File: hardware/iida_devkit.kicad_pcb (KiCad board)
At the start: 6 copper layers, 0 parts

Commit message: HW: Start laying out power section
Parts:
- added AE601: Antenna_Shield, iida-devkit:800MHz_PCB_ANT, F.Cu at (-138.3, 30.4)
- added C201: 1 µF, perfect_footprints:C_0201_0603Metric, F.Cu at (76.7, 38.3)
- added C202: 10 µF, Capacitor_SMD:C_0603_1608Metric, F.Cu at (-3.89, 23.7)
- added C203: 10 µF, Capacitor_SMD:C_0603_1608Metric, F.Cu at (2.71, 23.7)
- added C204: 4.7 µF, perfect_footprints:C_0402_1005Metric, F.Cu at (64.3, 75.9)
- added C205: 4.7 µF, perfect_footprints:C_0402_1005Metric, F.Cu at (66.9, 75.9)
- added C206: 100 µF, Capacitor_SMD:CP_Elec_6.3x3, F.Cu at (63.3, 30.8)
- added C207: 4.7 µF, perfect_footprints:C_0402_1005Metric, F.Cu at (70.4, 40.3)
- added C208: 1 µF, perfect_footprints:C_0201_0603Metric, F.Cu at (64.3, 79.5)
- added C209: 10 µF, Capacitor_SMD:C_0603_1608Metric, F.Cu at (67.8, 79.7)
- added C210: 10 µF, Capacitor_SMD:C_0603_1608Metric, F.Cu at (69.4, 79.7)
- added C211: 4.7 µF, perfect_footprints:C_0402_1005Metric, F.Cu at (69.6, 44.0)
- added C212: 1 µF, perfect_footprints:C_0201_0603Metric, F.Cu at (76.5, 81.6)
- added C213: 1 µF, perfect_footprints:C_0201_0603Metric, F.Cu at (66.4, 38.4)
- added C214: 22 µF, Capacitor_SMD:C_0603_1608Metric, F.Cu at (78.7, 79.8)
- added C215: 22 µF, Capacitor_SMD:C_0603_1608Metric, F.Cu at (80.3, 79.8)
- added C216: 22 µF, Capacitor_SMD:C_0603_1608Metric, F.Cu at (81.9, 79.8)
- added C301: 1 µF, perfect_footprints:C_0201_0603Metric, F.Cu at (-94.4, 96.2)
- added C302: 1 µF, perfect_footprints:C_0201_0603Metric, F.Cu at (-94.4, 97.8)
- added C303: 22 µF, Capacitor_SMD:C_0603_1608Metric, F.Cu at (-112.1, 103.3)
- added C304: 1 µF, perfect_footprints:C_0201_0603Metric, F.Cu at (-94.4, 99.4)
- added C305: 1 µF, perfect_footprints:C_0201_0603Metric, F.Cu at (-94.4, 101.0)
- added C306: 1 µF, perfect_footprints:C_0201_0603Metric, F.Cu at (-94.4, 102.7)
- added C307: 1 µF, perfect_footprints:C_0201_0603Metric, F.Cu at (-94.4, 104.3)
- added C308: 8 pF, perfect_footprints:C_0201_0603Metric, F.Cu at (-94.4, 105.9)
- added C309: 8 pF, perfect_footprints:C_0201_0603Metric, F.Cu at (-92.3, 96.2)
- added C310: 0.1 µF, perfect_footprints:C_0201_0603Metric, F.Cu at (-92.3, 97.8)
- added C311: 1 µF, perfect_footprints:C_0201_0603Metric, F.Cu at (-92.3, 99.4)
- added C312: 22 µF, Capacitor_SMD:C_0603_1608Metric, F.Cu at (-112.1, 105.8)
- added C313: 8 pF, perfect_footprints:C_0201_0603Metric, F.Cu at (-92.3, 101.0)
- added C314: 8 pF, perfect_footprints:C_0201_0603Metric, F.Cu at (-92.3, 102.7)
- added C315: 1 µF, perfect_footprints:C_0201_0603Metric, F.Cu at (-92.3, 104.3)
- added C401: 1 µF, perfect_footprints:C_0201_0603Metric, F.Cu at (-77.9, 89.0)
- added C402: 1 µF, perfect_footprints:C_0201_0603Metric, F.Cu at (-77.9, 90.7)
- added C403: 1 µF, perfect_footprints:C_0201_0603Metric, F.Cu at (-77.9, 92.3)
- added C404: 1 µF, perfect_footprints:C_0201_0603Metric, F.Cu at (-77.9, 93.9)
- added C405: 1 µF, perfect_footprints:C_0201_0603Metric, F.Cu at (-77.9, 95.5)
- added C501: 100 µF, Capacitor_SMD:CP_Elec_6.3x3, F.Cu at (-109.0, 68.4)
- added C502: 1 µF, perfect_footprints:C_0201_0603Metric, F.Cu at (-97.9, 64.1)
- added C503: 22 µF, Capacitor_SMD:C_0603_1608Metric, F.Cu at (-112.2, 73.7)
- added C504: 1 µF, perfect_footprints:C_0201_0603Metric, F.Cu at (-97.9, 65.7)
- added C505: 0.1 µF, perfect_footprints:C_0201_0603Metric, F.Cu at (-97.9, 67.3)
- added C506: 10000 pF, perfect_footprints:C_0201_0603Metric, F.Cu at (-97.9, 68.9)
- added C507: 1 µF, perfect_footprints:C_0201_0603Metric, F.Cu at (-97.9, 70.5)
- added C508: 100 pF, perfect_footprints:C_0201_0603Metric, F.Cu at (-97.9, 72.1)
- added C509: 10000 pF, perfect_footprints:C_0201_0603Metric, F.Cu at (-97.9, 73.7)
- added C510: 1 µF, perfect_footprints:C_0201_0603Metric, F.Cu at (-97.9, 75.3)
- added C511: 33 pF, perfect_footprints:C_0201_0603Metric, F.Cu at (-95.8, 64.1)
- added C512: 33 pF, perfect_footprints:C_0201_0603Metric, F.Cu at (-95.8, 65.7)
- added C513: 33 pF, perfect_footprints:C_0201_0603Metric, F.Cu at (-95.8, 67.3)
- added C601: 1.1 pF, perfect_footprints:C_0402_1005Metric, F.Cu at (-137.6, 32.9)
- added C602: 36 pF, perfect_footprints:C_0201_0603Metric, F.Cu at (-116.9, 32.7)
- added C603: 0.33 pF, perfect_footprints:C_0402_1005Metric, F.Cu at (-137.6, 34.9)
- added C604: 36 pF, perfect_footprints:C_0201_0603Metric, F.Cu at (-116.9, 34.3)
- added C605: 1.1 pF, perfect_footprints:C_0402_1005Metric, F.Cu at (-137.6, 36.8)
- added D201: SMAJ5.0A, Diode_SMD:D_SMA, F.Cu at (86.8, 30.8)
- added D202: SMAJ5.0A, Diode_SMD:D_SMA, F.Cu at (86.8, 43.0)
- added D203: DT1240A-08LP3810, Package_DFN_QFN:Diodes_UDFN3810-9_TYPE_B, F.Cu at (-7.19, 18.5)
- added D204: SMAJ5.0A, Diode_SMD:D_SMA, F.Cu at (0.31, 16.4)
- added D205: RED, LED_SMD:LED_0603_1608Metric, F.Cu at (71.3, 48.0)
- added D206: RED, LED_SMD:LED_0603_1608Metric, F.Cu at (-85.0, 141.7)
- added D207: RED, LED_SMD:LED_0603_1608Metric, F.Cu at (73.0, 48.0)
- added D208: RED, LED_SMD:LED_0603_1608Metric, F.Cu at (74.7, 48.0)
- added D401: RED, LED_SMD:LED_0603_1608Metric, F.Cu at (-66.4, 93.3)
- added D402: RED, LED_SMD:LED_0603_1608Metric, F.Cu at (-66.4, 95.9)
- added D403: RED, LED_SMD:LED_0603_1608Metric, F.Cu at (-66.4, 98.5)
- added D501: RED, LED_SMD:LED_0603_1608Metric, F.Cu at (-86.6, 70.5)
- added D502: RED, LED_SMD:LED_0603_1608Metric, F.Cu at (-86.6, 73.0)
- added D503: DT1240A-08LP3810, Package_DFN_QFN:Diodes_UDFN3810-9_TYPE_B, F.Cu at (-82.5, 66.1)
- added D601: DF2B5M4CT,L3F, Diode_SMD:D_SOD-882D, F.Cu at (-114.4, 33.0)
- added F201: 1.5 A, Fuse:Fuse_0805_2012Metric, F.Cu at (81.3, 42.2)
- added F202: 1.5 A, Fuse:Fuse_0805_2012Metric, F.Cu at (-0.63, 21.7)
- added FB501: BLM21BB201SH1D, Inductor_SMD:L_0805_2012Metric, F.Cu at (-101.5, 72.8)
- added FID101: Fiducial, Fiducial:Fiducial_1mm_Mask3mm, F.Cu at (-113.8, -81.4)
- added FID102: Fiducial, Fiducial:Fiducial_1mm_Mask3mm, F.Cu at (-113.8, -76.9)
- added FID103: Fiducial, Fiducial:Fiducial_1mm_Mask3mm, F.Cu at (-113.8, -72.3)
- added H101: MountingHole_Pad, MountingHole:MountingHole_5.3mm_M5_Pad_Via, F.Cu at (-122.2, -77.6)
- added H102: MountingHole_Pad, MountingHole:MountingHole_5.3mm_M5_Pad_Via, F.Cu at (-122.2, -65.5)
- added H103: MountingHole_Pad, MountingHole:MountingHole_5.3mm_M5_Pad_Via, F.Cu at (-122.2, -53.3)
- added H104: MountingHole_Pad, MountingHole:MountingHole_5.3mm_M5_Pad_Via, F.Cu at (-122.2, -41.2)
- added J201: B2B-XH-A, Connector_JST:JST_XH_B2B-XH-A_1x02_P2.50mm_Vertical, F.Cu at (84.8, 35.7)
- added J202: USB4105-GF-A, Connector_USB:USB_C_Receptacle_GCT_USB4105-xx-A_16P_TopMnt_Horizontal, F.Cu at (-7.99, 12.0)
- added J203: PRPC001DAAN-RC, Connector_PinHeader_2.54mm:PinHeader_1x02_P2.54mm_Vertical, F.Cu at (73.6, 27.3)
- added J204: PRPC001DAAN-RC, Connector_PinHeader_2.54mm:PinHeader_1x02_P2.54mm_Vertical, F.Cu at (3.68, 26.5)
- added J205: 61300111121, Connector_PinHeader_2.54mm:PinHeader_1x01_P2.54mm_Vertical, F.Cu at (73.9, 84.2)
- added J206: 61300111121, Connector_PinHeader_2.54mm:PinHeader_1x01_P2.54mm_Vertical, F.Cu at (-63.7, 145.9)
- added J207: 61300111121, Connector_PinHeader_2.54mm:PinHeader_1x01_P2.54mm_Vertical, F.Cu at (-63.7, 150.4)
- added J208: PRPC001DAAN-RC, Connector_PinHeader_2.54mm:PinHeader_1x02_P2.54mm_Vertical, F.Cu at (-87.6, 140.0)
- added J209: PRPC001DAAN-RC, Connector_PinHeader_2.54mm:PinHeader_1x02_P2.54mm_Vertical, F.Cu at (83.1, 75.9)
- added J301: TC2050, Connector:Tag-Connect_TC2050-IDC-NL_2x05_P1.27mm_Vertical_with_bottom_clip, F.Cu at (-113.1, 98.7)
- added J302: 61300611121, Connector_PinHeader_2.54mm:PinHeader_1x06_P2.54mm_Vertical, F.Cu at (-117.0, 80.4)
- added J303: 61300611121, Connector_PinHeader_2.54mm:PinHeader_1x06_P2.54mm_Vertical, F.Cu at (-112.4, 80.4)
- added J304: 61300611121, Connector_PinHeader_2.54mm:PinHeader_1x06_P2.54mm_Vertical, F.Cu at (-107.9, 80.4)
- added J305: 61300611121, Connector_PinHeader_2.54mm:PinHeader_1x06_P2.54mm_Vertical, F.Cu at (-103.3, 80.4)
- added J306: 61300611121, Connector_PinHeader_2.54mm:PinHeader_1x06_P2.54mm_Vertical, F.Cu at (-98.7, 80.4)
- added J501: SIM8066-6-1-14-01-A, GCT:SIM8066-6-1-14-01-A, F.Cu at (-106.6, 52.4)
- added J601: SMA 132134, Connector_Coaxial:SMA_Amphenol_132134-11_Vertical, F.Cu at (-122.6, 36.6)
- added JP301: SolderJumper_2_Open, Jumper:SolderJumper-2_P1.3mm_Open_TrianglePad1.0x1.5mm, F.Cu at (-104.6, 108.5)
- added L201: 1 µH, Inductor_SMD:L_Changjiang_FTC404020S, F.Cu at (73.9, 74.5)
- added L601: 36 nH, perfect_footprints:L_0402_1005Metric, F.Cu at (-137.6, 38.8)
- added L602: 1 nH, perfect_footprints:L_0402_1005Metric, F.Cu at (-134.7, 32.9)
- added L603: 110 nH, perfect_footprints:L_0402_1005Metric, F.Cu at (-134.7, 34.9)
- added L604: 1 nH, perfect_footprints:L_0402_1005Metric, F.Cu at (-134.7, 36.8)
- added L605: 36 nH, perfect_footprints:L_0402_1005Metric, F.Cu at (-134.7, 38.8)
- added Q201: IRLML6401, Package_TO_SOT_SMD:SOT-23-3, F.Cu at (79.1, 36.9)
- added Q202: DMN2005, Package_SON:Diodes_PowerDI3333-8, F.Cu at (74.5, 31.1)
- added Q203: DMN2005, Package_SON:Diodes_PowerDI3333-8, F.Cu at (70.2, 31.1)
- added Q301: BSS806NH, Package_TO_SOT_SMD:SOT-23-3, F.Cu at (-116.8, 108.8)
- added Q501: BSS806NH, Package_TO_SOT_SMD:SOT-23-3, F.Cu at (-116.8, 45.5)
- added Q502: IRLML6401, Package_TO_SOT_SMD:SOT-23-3, F.Cu at (-116.8, 49.9)
- added Q503: BSS806NH, Package_TO_SOT_SMD:SOT-23-3, F.Cu at (-116.8, 54.4)
- added Q504: BSS806NH, Package_TO_SOT_SMD:SOT-23-3, F.Cu at (-116.8, 58.8)
- added Q505: BSS806NH, Package_TO_SOT_SMD:SOT-23-3, F.Cu at (-116.8, 63.3)
- added Q506: BSS806NH, Package_TO_SOT_SMD:SOT-23-3, F.Cu at (-116.8, 67.7)
- added R101: 0 Ω, Resistor_SMD:R_1206_3216Metric, F.Cu at (-113.3, -68.4)
- added R201: 5.1 kΩ, perfect_footprints:R_0402_1005Metric, F.Cu at (-14.0, 15.8)
- added R202: 5.1 kΩ, perfect_footprints:R_0402_1005Metric, F.Cu at (-2.09, 15.8)
- added R203: 330 Ω, perfect_footprints:R_0201_0603Metric, F.Cu at (76.7, 37.6)
- added R204: 82 mΩ, Resistor_SMD:R_1206_3216Metric, F.Cu at (79.1, 31.5)
- added R205: 0 Ω, Resistor_SMD:R_0805_2012Metric, F.Cu at (-0.61, 23.7)
- added R206: 2.2 kΩ, perfect_footprints:R_0201_0603Metric, F.Cu at (75.6, 38.3)
- added R207: 180 kΩ, perfect_footprints:R_0201_0603Metric, F.Cu at (64.3, 80.2)
- added R208: 10 kΩ, perfect_footprints:R_0201_0603Metric, F.Cu at (73.8, 39.1)
- added R209: 2.2 kΩ, perfect_footprints:R_0201_0603Metric, F.Cu at (73.8, 40.5)
- added R210: 0 Ω, perfect_footprints:R_0201_0603Metric, F.Cu at (70.9, 80.7)
- added R211: 0 Ω, perfect_footprints:R_0201_0603Metric, F.Cu at (71.6, 80.7)
- added R212: 2.2 kΩ, perfect_footprints:R_0201_0603Metric, F.Cu at (71.8, 45.8)
- added R213: 2.2 kΩ, perfect_footprints:R_0201_0603Metric, F.Cu at (-85.0, 139.6)
- added R214: 2.2 kΩ, perfect_footprints:R_0201_0603Metric, F.Cu at (72.5, 45.8)
- added R215: 2.2 kΩ, perfect_footprints:R_0201_0603Metric, F.Cu at (73.8, 39.8)
- added R216: 1.02 MΩ, perfect_footprints:R_0201_0603Metric, F.Cu at (77.6, 79.6)
- added R217: 180 kΩ, perfect_footprints:R_0201_0603Metric, F.Cu at (76.9, 80.2)
- added R218: 22 Ω, perfect_footprints:R_0201_0603Metric, F.Cu at (64.0, 41.4)
- added R219: 0 Ω, Resistor_SMD:R_0805_2012Metric, F.Cu at (84.4, 78.7)
- added R301: 180 kΩ, perfect_footprints:R_0201_0603Metric, F.Cu at (-92.3, 105.9)
- added R302: 10 kΩ, perfect_footprints:R_0201_0603Metric, F.Cu at (-90.3, 96.2)
- added R303: 330 Ω, perfect_footprints:R_0201_0603Metric, F.Cu at (-90.3, 97.8)
- added R304: 330 Ω, perfect_footprints:R_0201_0603Metric, F.Cu at (-90.3, 99.4)
- added R305: 2.2 kΩ, perfect_footprints:R_0201_0603Metric, F.Cu at (-90.3, 101.0)
- added R306: 2.2 kΩ, perfect_footprints:R_0201_0603Metric, F.Cu at (-90.3, 102.7)
- added R307: 10 kΩ, perfect_footprints:R_0201_0603Metric, F.Cu at (-90.3, 104.3)
- added R308: 10 kΩ, perfect_footprints:R_0201_0603Metric, F.Cu at (-90.3, 105.9)
- added R309: 22 Ω, perfect_footprints:R_0201_0603Metric, F.Cu at (-88.2, 96.2)
- added R310: 22 Ω, perfect_footprints:R_0201_0603Metric, F.Cu at (-88.2, 97.8)
- added R311: 22 Ω, perfect_footprints:R_0201_0603Metric, F.Cu at (-88.2, 99.4)
- added R312: 22 Ω, perfect_footprints:R_0201_0603Metric, F.Cu at (-88.2, 101.0)
- added R313: 22 Ω, perfect_footprints:R_0201_0603Metric, F.Cu at (-88.2, 102.7)
- added R314: 22 Ω, perfect_footprints:R_0201_0603Metric, F.Cu at (-88.2, 104.3)
- added R315: 22 Ω, perfect_footprints:R_0201_0603Metric, F.Cu at (-88.2, 105.9)
- added R316: 22 Ω, perfect_footprints:R_0201_0603Metric, F.Cu at (-86.1, 96.2)
- added R317: 22 Ω, perfect_footprints:R_0201_0603Metric, F.Cu at (-86.1, 97.8)
- added R318: 0 Ω, Resistor_SMD:R_0805_2012Metric, F.Cu at (-111.9, 108.5)
- added R319: 22 Ω, perfect_footprints:R_0201_0603Metric, F.Cu at (-86.1, 99.4)
- added R320: 330 Ω, perfect_footprints:R_0201_0603Metric, F.Cu at (-86.1, 101.0)
- added R321: 10 kΩ, perfect_footprints:R_0201_0603Metric, F.Cu at (-86.1, 102.7)
- added R401: 180 kΩ, perfect_footprints:R_0201_0603Metric, F.Cu at (-77.9, 97.1)
- added R402: 22 Ω, perfect_footprints:R_0201_0603Metric, F.Cu at (-77.9, 98.7)
- added R403: 22 Ω, perfect_footprints:R_0201_0603Metric, F.Cu at (-75.8, 89.0)
- added R404: 22 Ω, perfect_footprints:R_0201_0603Metric, F.Cu at (-75.8, 90.7)
- added R405: 22 Ω, perfect_footprints:R_0201_0603Metric, F.Cu at (-75.8, 92.3)
- added R406: 22 Ω, perfect_footprints:R_0201_0603Metric, F.Cu at (-75.8, 93.9)
- added R407: 22 Ω, perfect_footprints:R_0201_0603Metric, F.Cu at (-75.8, 95.5)
- added R408: 22 Ω, perfect_footprints:R_0201_0603Metric, F.Cu at (-75.8, 97.1)
- added R409: 22 Ω, perfect_footprints:R_0201_0603Metric, F.Cu at (-75.8, 98.7)
- added R410: 2.2 kΩ, perfect_footprints:R_0201_0603Metric, F.Cu at (-73.8, 89.0)
- added R411: 2.2 kΩ, perfect_footprints:R_0201_0603Metric, F.Cu at (-73.8, 90.7)
- added R412: 2.2 kΩ, perfect_footprints:R_0201_0603Metric, F.Cu at (-73.8, 92.3)
- added R413: 180 kΩ, perfect_footprints:R_0201_0603Metric, F.Cu at (-73.8, 93.9)
- added R414: 180 kΩ, perfect_footprints:R_0201_0603Metric, F.Cu at (-73.8, 95.5)
- added R415: 22 Ω, perfect_footprints:R_0201_0603Metric, F.Cu at (-73.8, 97.1)
- added R416: 180 kΩ, perfect_footprints:R_0201_0603Metric, F.Cu at (-73.8, 98.7)
- added R501: 180 kΩ, perfect_footprints:R_0201_0603Metric, F.Cu at (-95.8, 68.9)
- added R502: 180 kΩ, perfect_footprints:R_0201_0603Metric, F.Cu at (-95.8, 70.5)
- added R503: 330 Ω, perfect_footprints:R_0201_0603Metric, F.Cu at (-95.8, 72.1)
- added R504: 0 Ω, Resistor_SMD:R_0805_2012Metric, F.Cu at (-86.4, 64.7)
- added R505: 0 Ω, Resistor_SMD:R_0805_2012Metric, F.Cu at (-86.4, 67.7)
- added R506: 180 kΩ, perfect_footprints:R_0201_0603Metric, F.Cu at (-95.8, 73.7)
- added R507: 330 Ω, perfect_footprints:R_0201_0603Metric, F.Cu at (-95.8, 75.3)
- added R508: 330 Ω, perfect_footprints:R_0201_0603Metric, F.Cu at (-93.8, 64.1)
- added R509: 22 Ω, perfect_footprints:R_0201_0603Metric, F.Cu at (-93.8, 65.7)
- added R510: 22 Ω, perfect_footprints:R_0201_0603Metric, F.Cu at (-93.8, 67.3)
- added R511: 22 Ω, perfect_footprints:R_0201_0603Metric, F.Cu at (-93.8, 68.9)
- added R512: 22 Ω, perfect_footprints:R_0201_0603Metric, F.Cu at (-93.8, 70.5)
- added R513: 180 kΩ, perfect_footprints:R_0201_0603Metric, F.Cu at (-93.8, 72.1)
- added R514: 330 Ω, perfect_footprints:R_0201_0603Metric, F.Cu at (-93.8, 73.7)
- added R515: 180 kΩ, perfect_footprints:R_0201_0603Metric, F.Cu at (-93.8, 75.3)
- added R516: 22 Ω, perfect_footprints:R_0201_0603Metric, F.Cu at (-91.7, 64.1)
- added R517: 22 Ω, perfect_footprints:R_0201_0603Metric, F.Cu at (-91.7, 65.7)
- added R518: 22 Ω, perfect_footprints:R_0201_0603Metric, F.Cu at (-91.7, 67.3)
- added R519: 180 kΩ, perfect_footprints:R_0201_0603Metric, F.Cu at (-91.7, 68.9)
- added R520: 330 Ω, perfect_footprints:R_0201_0603Metric, F.Cu at (-91.7, 70.5)
- added R521: 2.2 kΩ, perfect_footprints:R_0201_0603Metric, F.Cu at (-91.7, 72.1)
- added R522: 180 kΩ, perfect_footprints:R_0201_0603Metric, F.Cu at (-91.7, 73.7)
- added R523: 330 Ω, perfect_footprints:R_0201_0603Metric, F.Cu at (-91.7, 75.3)
- added R524: 2.2 kΩ, perfect_footprints:R_0201_0603Metric, F.Cu at (-89.6, 64.1)
- added R525: 180 kΩ, perfect_footprints:R_0201_0603Metric, F.Cu at (-89.6, 65.7)
- added R526: 180 kΩ, perfect_footprints:R_0201_0603Metric, F.Cu at (-89.6, 67.3)
- added R601: 0 Ω, perfect_footprints:R_0402_1005Metric, F.Cu at (-131.7, 32.9)
- added R602: 0 Ω, perfect_footprints:R_0402_1005Metric, F.Cu at (-131.7, 34.9)
- added R603: 0 Ω, perfect_footprints:R_0402_1005Metric, F.Cu at (-131.7, 36.8)
- added R604: 0 Ω, perfect_footprints:R_0402_1005Metric, F.Cu at (-131.7, 38.8)
- added R605: 0 Ω, perfect_footprints:R_0402_1005Metric, F.Cu at (-128.8, 32.9)
- added R606: 0 Ω, perfect_footprints:R_0402_1005Metric, F.Cu at (-128.8, 34.9)
- added R607: 0 Ω, perfect_footprints:R_0402_1005Metric, F.Cu at (-128.8, 36.8)
- added R608: 0 Ω, perfect_footprints:R_0402_1005Metric, F.Cu at (-128.8, 38.8)
- added SW301: PTS645S, Button_Switch_SMD:SW_SPST_PTS645Sx43SMTR92, F.Cu at (-90.8, 82.1)
- added SW302: PTS645S, Button_Switch_SMD:SW_SPST_PTS645Sx43SMTR92, F.Cu at (-90.8, 89.9)
- added TP201: TestPoint, TestPoint:TestPoint_Pad_D1.0mm, B.Cu at (76.0, 30.1)
- added TP202: TestPoint, TestPoint:TestPoint_Pad_D1.0mm, B.Cu at (69.4, 29.4)
- added TP203: TestPoint, TestPoint:TestPoint_Pad_D1.0mm, B.Cu at (80.3, 77.2)
- added TP204: TestPoint, TestPoint:TestPoint_Pad_D1.0mm, B.Cu at (-1.69, 26.5)
- added TP205: TestPoint, TestPoint:TestPoint_Pad_D1.0mm, B.Cu at (63.3, 36.6)
- added U201: BQ29728DSER, Package_SON:WSON-6_1.5x1.5mm_P0.5mm, F.Cu at (76.4, 39.9)
- added U202: LM66200DRLR, Package_TO_SOT_SMD:SOT-583-8, F.Cu at (65.6, 77.8)
- added U203: MCP73833T-FCI/MF, Package_DFN_QFN:DFN-10-1EP_3x3mm_P0.5mm_EP1.58x2.35mm, F.Cu at (71.9, 43.0)
- added U204: TPS63020DSJR, Texas Instruments:TPS6302xDSJ, F.Cu at (73.9, 79.4)
- added U205: MAX17048G+T10, Package_DFN_QFN:TDFN-8-1EP_2x2mm_P0.5mm_EP0.8x1.2mm, F.Cu at (65.9, 40.4)
- added U301: STM32L552CET6, Package_QFP:LQFP-48_7x7mm_P0.5mm, F.Cu at (-101.5, 100.4)
- added U401: TCA9554PW, Package_SO:TSSOP-16_4.4x5mm_P0.65mm, F.Cu at (-74.2, 84.9)
- added U402: AT25SF081B-MAHB-T, Package_DFN_QFN:DFN-8-1EP_2x3mm_P0.5mm_EP0.61x2.2mm, F.Cu at (-70.6, 94.3)
- added U403: MCP9808T-E/MC, Package_DFN_QFN:DFN-8-1EP_3x2mm_P0.5mm_EP1.75x1.45mm, F.Cu at (-69.9, 90.2)
- added U404: M24256E-B, Package_SO:SOIC-8_3.9x4.9mm_P1.27mm, F.Cu at (-65.6, 85.0)
- added U405: SHT40-AD1B-R2, Sensor_Humidity:Sensirion_DFN-4_1.5x1.5mm_P0.8mm_SHT4x_NoCentralPad, F.Cu at (-70.7, 98.1)
- added U501: TXS0108E, Package_DFN_QFN:DHVQFN-20-1EP_2.5x4.5mm_P0.5mm_EP1x3mm, F.Cu at (-101.4, 68.0)
- added U502: BG770AGLAA-N06-SGNSA, Quectel:Quectel_BG77, F.Cu at (-89.9, 53.3)
- added Y301: ECS-160-9-37-CKM-TR3, Crystal:Crystal_SMD_3225-4Pin_3.2x2.5mm, F.Cu at (-116.7, 104.3)
- added Y302: ABS05-32.768KHZ-9-T, Crystal:Crystal_SMD_MicroCrystal_CM9V-T1A-2Pin_1.6x1.0mm, F.Cu at (-100.6, 108.3)
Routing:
- net CHASSIS: track 0.00 -> 33.8 mm, vias 0 -> 1
- net /Power/V_BUS_IN: track 0.00 -> 26.7 mm, vias 0 -> 2
- net /Power/C_{OUT}: track 0.00 -> 23.9 mm, vias 0 -> 2
- net /Power/D_{OUT}: track 0.00 -> 18.2 mm, vias 0 -> 2
- net /Power/VINA: track 0.00 -> 12.2 mm
- net /Power/CC1: track 0.00 -> 8.13 mm
- net Net-(D208-K): track 0.00 -> 7.92 mm
- net /Power/V_BUS: track 0.00 -> 7.48 mm, vias 0 -> 1
- net GND: track 0.00 -> 7.32 mm, vias 0 -> 85
- net /Microcontroller/USB.D+: track 0.00 -> 7.26 mm
- net /Power/CC2: track 0.00 -> 7.21 mm
- net /Microcontroller/USB.D-: track 0.00 -> 6.27 mm
- net /Power/GND_BAT: track 0.00 -> 4.34 mm
- net /Power/THERM: track 0.00 -> 3.85 mm
- net /Microcontroller/I2C.SCL: track 0.00 -> 3.46 mm, vias 0 -> 1
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- added copper zone on F.Cu, net /Power/GND_BAT
- added copper zone on F.Cu, net /Power/V_BAT
- added copper zone on F.Cu, net /Power/V_BAT_IN
- added copper zone on F.Cu, net /Power/V_OUT
- added copper zone on F.Cu, net /Power/V_SYS
- added copper zone on B.Cu, net GND
- added copper zone on F.Cu, net GND
- added copper zone on In1.Cu, net GND
- added copper zone on In3.Cu, net GND
- added copper zone on In4.Cu, net GND
- added copper zone on F.Cu, net Net-(J203-Pin_1)
- added copper zone on F.Cu, net Net-(L201-Pad1)
- added copper zone on F.Cu, net Net-(L201-Pad2)
- added copper zone on F.Cu, net Net-(Q201-D)
- added copper zone on F.Cu, net Net-(Q202-D)
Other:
- board text added: "+5V"
- board text added: "BAT+"
- board text added: "BAT-"
- board text added: "GND"

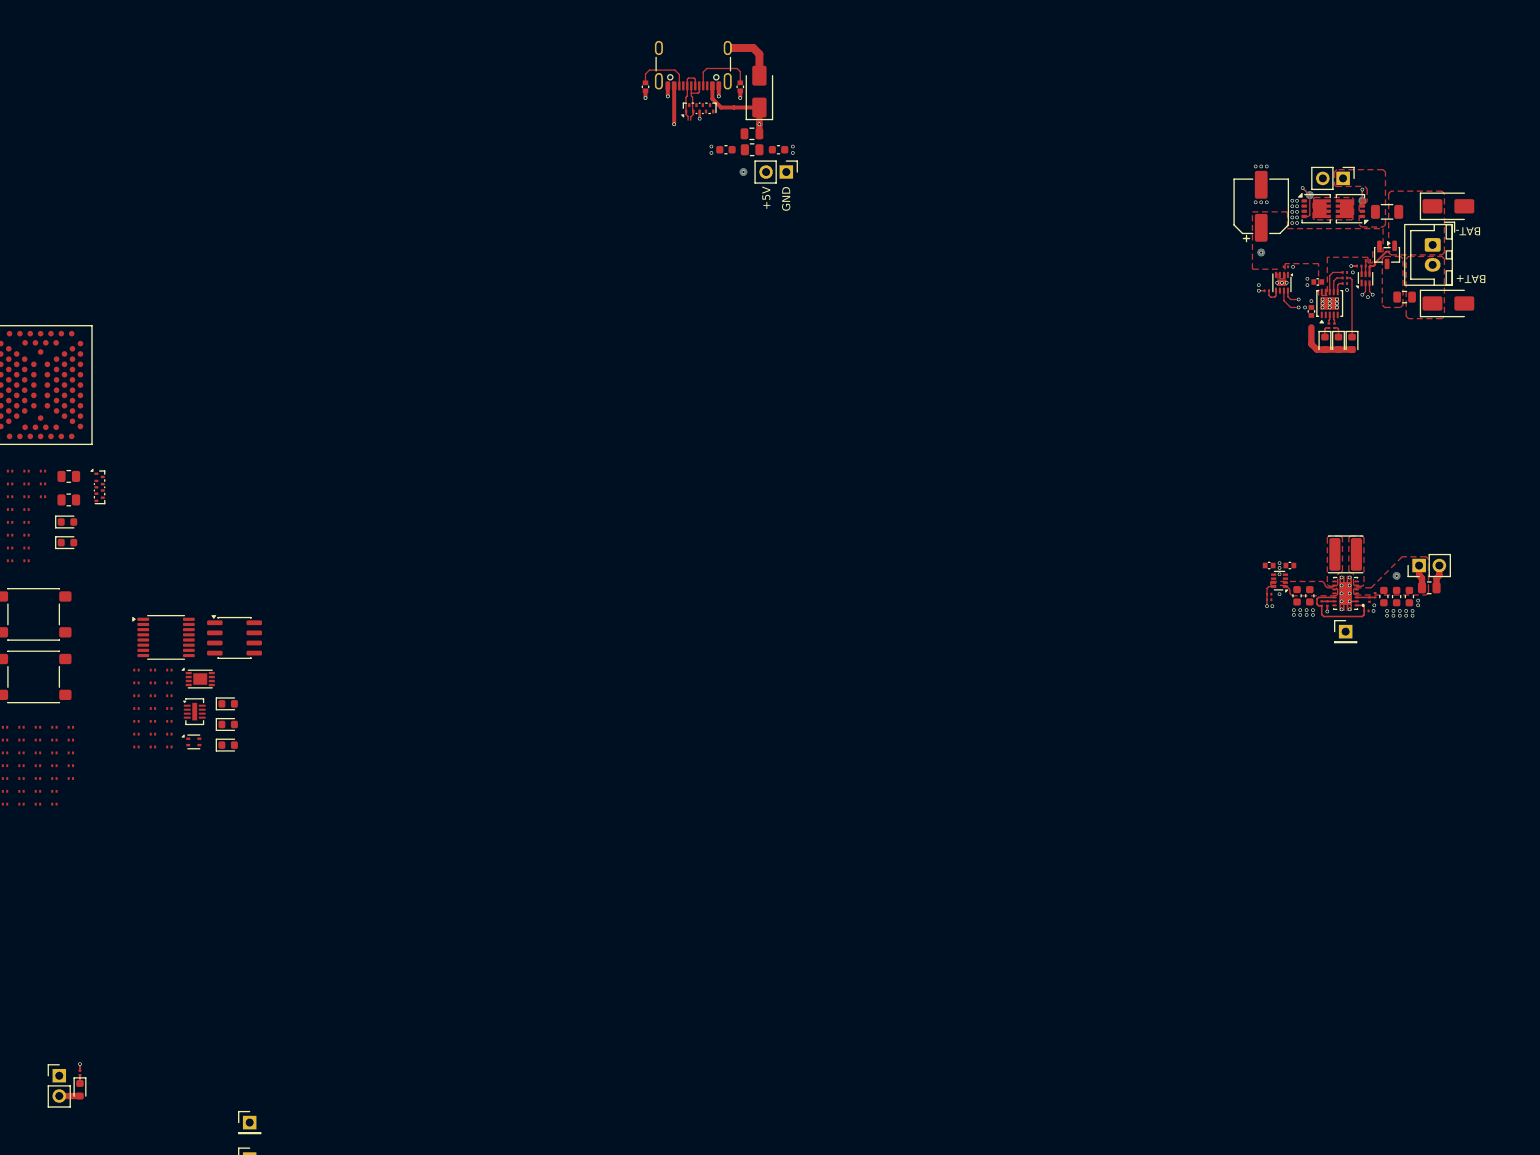
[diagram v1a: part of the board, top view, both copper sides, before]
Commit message: HW: Finish power layout
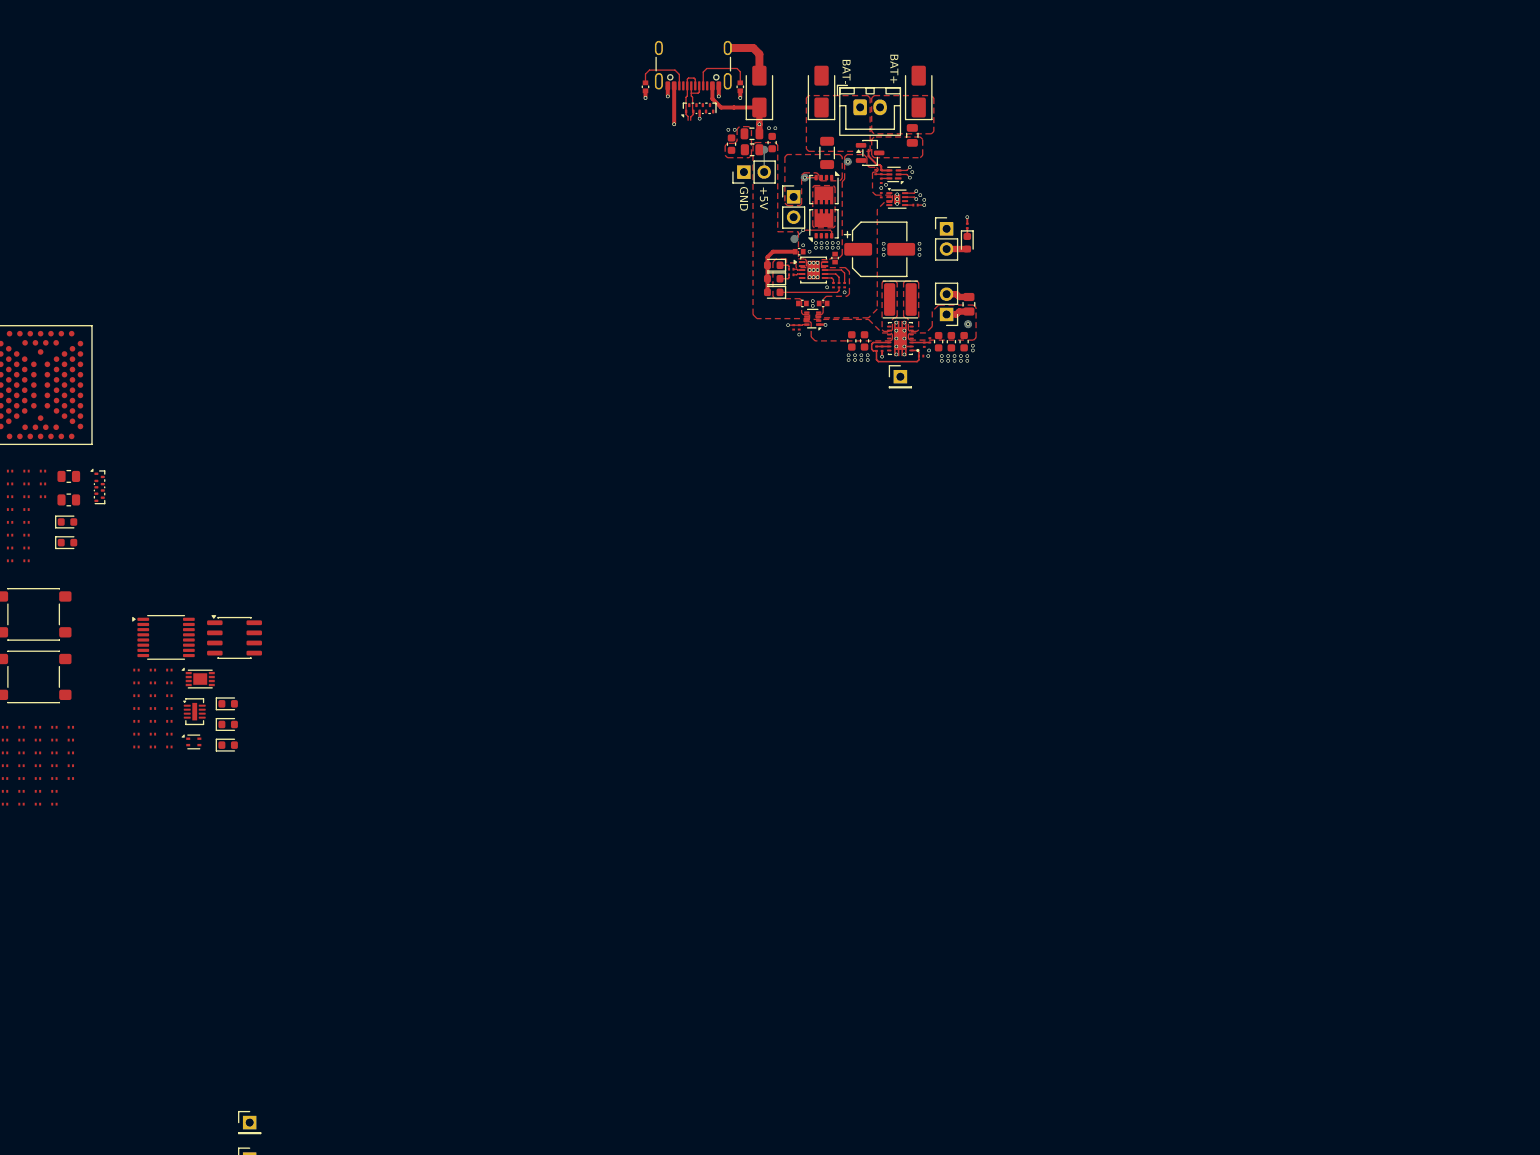
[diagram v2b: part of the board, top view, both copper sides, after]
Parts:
- moved D206 154.0 mm to (26.4, 35.4)
- moved J208 154.0 mm to (23.8, 33.6)
- moved R213 154.0 mm to (26.4, 33.3)
- moved D201 80.0 mm to (8.11, 16.4), turned to 90 degrees
- moved J201 73.9 mm to (13.0, 18.4), turned to 0 degrees
- moved D208 72.9 mm to (2.11, 41.6), turned to 180 degrees
- moved D202 71.6 mm to (20.3, 16.4), turned to 90 degrees
- moved D207 71.4 mm to (2.11, 39.9), turned to 180 degrees
- moved R204 70.7 mm to (8.81, 24.1), turned to -90 degrees
- moved TP201 70.1 mm to (6.01, 27.2), turned to 0 degrees
- moved D205 69.9 mm to (2.11, 38.2), turned to 180 degrees
- moved J203 69.0 mm to (4.61, 29.6), turned to 0 degrees
- moved R207 68.8 mm to (4.61, 46.0), turned to 90 degrees
- moved R214 68.5 mm to (4.31, 39.4), turned to 0 degrees
- moved R219 67.9 mm to (26.6, 43.1), turned to 90 degrees
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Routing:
- net /Power/V_BUS: track 7.48 -> 11.0 mm, vias 1 -> 0
- net /Power/C_{OUT}: track 23.9 -> 26.5 mm
- net /Microcontroller/I2C.SCL: track 3.46 -> 1.52 mm
- net Net-(U205-~{ALRT}): track 2.27 -> 1.04 mm
- net /Microcontroller/ST: track 3.15 -> 2.39 mm
- net /Microcontroller/I2C.SDA: track 2.26 -> 1.52 mm
- net GND: track 7.32 -> 7.47 mm, vias 85 -> 83
- added copper zone on F.Cu, net /Power/V_BUS
- added copper zone on F.Cu, net Net-(C202-Pad1)

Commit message: HW: Start laying out the microcontroller
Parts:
- moved C303 173.0 mm to (57.2, 67.4), turned to 180 degrees
- moved R318 169.5 mm to (54.3, 75.3), turned to -90 degrees
- moved Y301 169.3 mm to (48.9, 69.3), turned to -90 degrees
- moved C312 167.3 mm to (52.5, 75.5), turned to 90 degrees
- moved U301 165.9 mm to (62.0, 72.0)
- moved C305 163.9 mm to (66.2, 68.2), turned to 90 degrees
- moved C306 162.4 mm to (65.8, 76.2)
- moved R314 160.2 mm to (69.0, 73.3), turned to 180 degrees
- moved R313 158.7 mm to (67.8, 73.8), turned to 180 degrees
- moved R308 157.7 mm to (61.1, 61.6), turned to 180 degrees
- moved R307 157.5 mm to (61.1, 60.9)
- moved C304 156.4 mm to (58.4, 66.3), turned to 180 degrees
- moved Y302 156.2 mm to (49.7, 65.7), turned to -90 degrees
- moved R317 156.0 mm to (67.8, 72.3)
- moved R305 155.3 mm to (60.5, 64.0)
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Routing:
- net /Microcontroller/LSE_IN: track 0.00 -> 11.3 mm
- net /Microcontroller/HSE_IN: track 0.00 -> 11.1 mm
- net /Microcontroller/LSE_OUT: track 0.00 -> 10.8 mm
- net /Microcontroller/HSE_OUT: track 0.00 -> 8.65 mm
- net /Microcontroller/BOOT0: track 0.00 -> 6.99 mm
- net /Microcontroller/IO_EXP_INTn: track 0.00 -> 5.52 mm, vias 0 -> 1
- net V_3V3: track 2.95 -> 7.58 mm, vias 0 -> 13
- net /Microcontroller/GPIO_PA0: track 0.00 -> 4.21 mm
- net /Microcontroller/RESETn: track 0.00 -> 4.09 mm
- net /Microcontroller/I2C.SCL: track 1.52 -> 5.39 mm
- net /Microcontroller/GPIO_PA1: track 0.00 -> 3.38 mm
- net /Microcontroller/I2C.SDA: track 1.52 -> 4.90 mm
- net Net-(SW302-A): track 0.00 -> 2.75 mm
- net Net-(Q301-D): track 0.00 -> 2.59 mm
- net Net-(U301-PB15): track 0.00 -> 2.58 mm
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- added copper zone on F.Cu, net /Microcontroller/V_DDA
- added copper zone on F.Cu, net V_3V3

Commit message: HW: Layout peripherals
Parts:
- moved C404 141.7 mm to (59.0, 57.4), turned to 90 degrees
- moved C405 139.7 mm to (55.0, 52.4), turned to 180 degrees
- moved R405 139.6 mm to (63.5, 83.6), turned to 180 degrees
- moved R404 139.5 mm to (63.5, 84.3), turned to 180 degrees
- moved R416 138.6 mm to (59.0, 59.0), turned to -90 degrees
- moved C402 137.4 mm to (59.4, 85.7), turned to -90 degrees
- moved R403 134.5 mm to (58.5, 83.1)
- moved R406 134.3 mm to (58.1, 84.3)
- moved R415 134.1 mm to (53.2, 53.8), turned to 180 degrees
- moved R414 133.9 mm to (53.2, 53.1)
- moved U405 133.2 mm to (55.0, 54.0), turned to 90 degrees
- moved U402 132.0 mm to (61.0, 84.0), turned to 180 degrees
- moved C403 131.2 mm to (47.8, 54.6), turned to 90 degrees
- moved R401 129.1 mm to (46.6, 63.0), turned to 90 degrees
- moved R402 128.7 mm to (45.7, 62.7), turned to 180 degrees
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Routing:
- net /Microcontroller/I2C.SCL: track 5.39 -> 35.3 mm, vias 1 -> 4
- net /Microcontroller/I2C.SDA: track 4.90 -> 32.1 mm
- net /Peripherals/TEMP_INTn: track 0.00 -> 23.1 mm
- net /Microcontroller/FLASH_QSPI.SCK: track 0.00 -> 14.2 mm
- net /Microcontroller/FLASH_QSPI.IO1: track 0.00 -> 13.5 mm
- net /Microcontroller/FLASH_QSPI.IO2: track 0.00 -> 13.4 mm
- net /Microcontroller/FLASH_QSPI.IO3: track 0.00 -> 11.3 mm, vias 0 -> 2
- net /Microcontroller/EEPROM_WCn: track 0.00 -> 10.5 mm
- net /Microcontroller/IO_EXP_INTn: track 5.52 -> 16.0 mm, vias 1 -> 0
- net /Microcontroller/FLASH_QSPI.IO0: track 0.00 -> 10.5 mm, vias 0 -> 2
- net /Microcontroller/FLASH_QSPI.CSn: track 0.00 -> 9.65 mm, vias 0 -> 2
- net Net-(D403-K): track 0.00 -> 6.69 mm
- net Net-(D402-K): track 0.00 -> 4.82 mm
- net V_3V3: track 7.58 -> 12.3 mm, vias 13 -> 23
- net /Peripherals/BAT_MON_INTn: track 0.83 -> 5.04 mm, vias 1 -> 2
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
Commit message: HW: Fix DRC errors
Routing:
- net /Microcontroller/GPIO_PA0: track 4.21 -> 0.00 mm
- net /Microcontroller/GPIO_PA1: track 3.38 -> 0.00 mm
- net /Microcontroller/GPIO_PA2: track 2.44 -> 0.00 mm
- net /Power/D_{OUT}: track 18.2 -> 16.8 mm
- net /Microcontroller/USB.D-: track 6.27 -> 5.03 mm
- net /Microcontroller/USB.D+: track 7.26 -> 6.06 mm
- net GND: vias 140 -> 128

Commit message: HW: Refine layouts
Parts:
- moved Q301 185.8 mm to (102.5, 77.0), turned to -90 degrees
- moved C302 183.1 mm to (103.2, 79.7)
- moved R301 183.0 mm to (102.5, 79.7), turned to 90 degrees
- moved R304 180.8 mm to (101.8, 79.7), turned to -90 degrees
- moved J301 179.5 mm to (65.0, 121.0), turned to 90 degrees
- moved R302 126.9 mm to (42.5, 148.5)
- moved SW301 126.9 mm to (37.0, 151.0)
- moved SW302 119.7 mm to (28.3, 149.3), turned to 90 degrees
- moved R321 111.3 mm to (25.8, 143.9), turned to 0 degrees
- moved C315 110.9 mm to (26.3, 143.2), turned to 0 degrees
- moved R320 109.6 mm to (26.1, 142.3), turned to -90 degrees
- moved JP301 106.9 mm to (26.1, 140.0), turned to -90 degrees
- moved C304 67.0 mm to (58.4, 133.3)
- moved C305 67.0 mm to (66.2, 135.2)
- moved C306 67.0 mm to (65.8, 143.2)
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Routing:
- net /Power/V_BUS: track 11.0 -> 0.00 mm, vias 0 -> 1
- net /Power/V_BAT: track 0.00 -> 6.79 mm, vias 1 -> 2
- net GND: track 9.71 -> 9.16 mm
- net /Microcontroller/ST: track 2.39 -> 2.70 mm, vias 1 -> 0
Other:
- board text added: "V_3V3"

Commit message: HW: Start laying out the modem
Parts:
- moved Q501 343.5 mm to (221.0, 107.7), turned to 90 degrees
- moved Q502 339.4 mm to (218.1, 105.0), turned to 180 degrees
- moved Q503 331.1 mm to (209.0, 113.7), turned to 90 degrees
- moved Q504 326.9 mm to (205.5, 113.7), turned to 90 degrees
- moved C503 326.9 mm to (213.4, 103.0)
- moved C501 326.1 mm to (214.4, 110.4), turned to -90 degrees
- moved J501 320.5 mm to (203.6, 133.0)
- moved R501 319.6 mm to (221.7, 105.0), turned to 90 degrees
- moved R502 319.1 mm to (220.8, 110.4), turned to 90 degrees
- moved R507 318.2 mm to (221.0, 105.0), turned to -90 degrees
- moved R503 318.2 mm to (220.1, 110.4), turned to 90 degrees
- moved FB501 316.8 mm to (213.7, 104.7), turned to 180 degrees
- moved C504 312.1 mm to (211.6, 105.5), turned to -90 degrees
- moved C505 311.5 mm to (211.6, 102.4), turned to 90 degrees
- moved C506 311.0 mm to (210.9, 105.5), turned to -90 degrees
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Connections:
- D503 pad 1: /Modem/SIM_DET -> /Modem/SIM_CLK
- D503 pad 4: /Modem/SIM_CLK -> /Modem/V_1V8_SIM
- D503 pad 5: /Modem/SIM_DATA -> /Modem/SIM_DET
- D503 pad 6: /Modem/V_1V8_SIM -> unconnected-(D503-Line-7-Pad6)
- D503 pad 9: unconnected-(D503-Line-2-Pad9) -> /Modem/SIM_DATA
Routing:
- net CHASSIS: track 33.8 -> 74.9 mm, vias 1 -> 4
- net /Modem/V_1V8_SIM: track 0.00 -> 23.3 mm, vias 0 -> 2
- net /Modem/SIM_DET: track 0.00 -> 22.1 mm, vias 0 -> 2
- net /Modem/SIM_CLK: track 0.00 -> 16.1 mm
- net /Modem/SIM_RST: track 0.00 -> 14.4 mm, vias 0 -> 2
- net /Modem/MDM_PWR_ON: track 2.09 -> 16.2 mm, vias 1 -> 3
- net /Modem/SIM_DATA: track 0.00 -> 13.9 mm
- net /Modem/PWRKEY: track 0.00 -> 9.28 mm
- net /Modem/MDM_RESET: track 0.60 -> 9.76 mm, vias 1 -> 3
- net /Microcontroller/MDM_RTS: track 0.00 -> 8.11 mm, vias 0 -> 1
- net /Microcontroller/MDM_DTR: track 0.00 -> 7.98 mm, vias 0 -> 1
- net Net-(U501-B7): track 0.00 -> 7.98 mm
- net /Modem/RESETn: track 0.00 -> 6.72 mm
- net Net-(U502-USIM_RST): track 0.00 -> 4.44 mm
- net Net-(U502-USIM_DATA): track 0.00 -> 4.31 mm
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- added copper zone on F.Cu, net /Modem/V_1V8_MDM
- added copper zone on F.Cu, net /Modem/V_3V3_MDM
- added copper zone on F.Cu, net /Modem/V_3V3_MDM_RAW
